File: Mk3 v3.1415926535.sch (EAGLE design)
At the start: 150 parts, among them IC1 TPD3E001DRL, IC2 TPS62082, IC3 STM32F401V, IC4 BQ24092, IC6 CC3100MOD, IC7 BQ2970, IC8 LSM6DS3, IC9 LIS3MDL, J1 ZX62-AB-5PA(11), J2 ER-CON50HT-1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

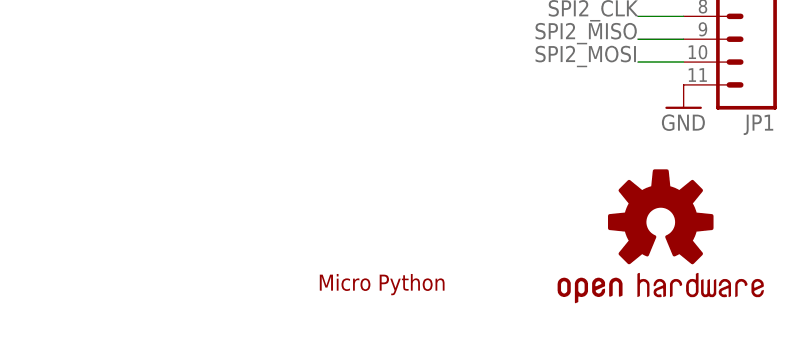
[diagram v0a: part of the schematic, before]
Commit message: Sponsor logos to rear Note this moves the files to Eagle 7
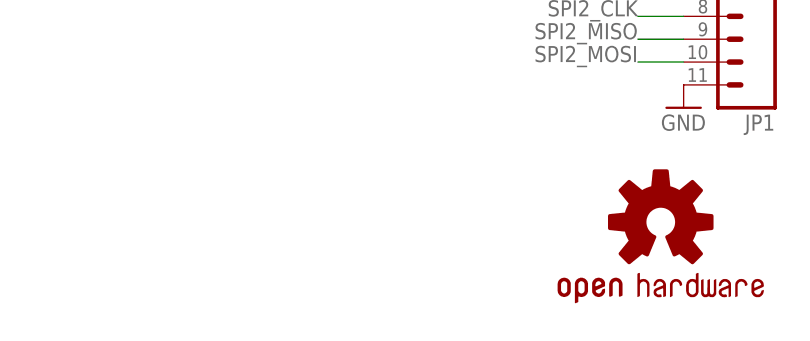
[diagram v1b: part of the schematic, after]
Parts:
- removed LOGO3: MICROPYTHON-SILK, TiLDA Mk3 Parts:MICROPYTHON-SILK
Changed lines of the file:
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@@
 <?xml version="1.0" encoding="utf-8"?>
 <!DOCTYPE eagle SYSTEM "eagle.dtd">
-<eagle version="6.6.0">
+<eagle version="7.5.0">
 <drawing>
 <settings>
@@
 <setting verticaltext="up"/>
 </settings>
-<grid distance="0.1" unitdist="inch" unit="inch" style="lines" multiple="1" display="no" altdistance="0.025" altunitdist="inch" altunit="inch"/>
+<grid distance="0.1" unitdist="inch" unit="inch" style="lines" multiple="1" display="no" altdistance="0.01" altunitdist="inch" altunit="inch"/>
 <layers>
 <layer number="1" name="Top" color="4" fill="1" visible="no" active="no"/>
@@
 <part name="+3V21" library="supply1" deviceset="+3V3" device=""/>
 <part name="OUTLINE1" library="TiLDA Mk3 Parts" deviceset="TILDA_MK3_BOARDOUTLINE" device="">
-<variant name="L4" populate="no"/>
-</part>
-<part name="LOGO3" library="TiLDA Mk3 Parts" deviceset="MICROPYTHON" device="-SILK" value="MICROPYTHON-SILK">
 <variant name="L4" populate="no"/>
 </part>
@@
 <instance part="+3V21" gate="G$1" x="210.82" y="40.64" rot="R90"/>
 <instance part="OUTLINE1" gate="G$1" x="502.92" y="27.94"/>
-<instance part="LOGO3" gate="G$1" x="292.1" y="7.62"/>
 <instance part="U2" gate="G$1" x="718.82" y="185.42"/>
 <instance part="R32" gate="G$1" x="647.7" y="134.62" smashed="yes" rot="R90">

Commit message: Lots of clean up in schematic
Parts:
- added LOGO2: LOGO_TI-4MM, TiLDA Mk3 Parts:LOGO_TI-4MM
- added LOGO3: LOGO_ST-4MM, TiLDA Mk3 Parts:LOGO_ST-4MM
- added LOGO4: LOGO_HCD-4MM, TiLDA Mk3 Parts:LOGO_HCD-4MM
- added LOGO5: LOGO_MICROSOFT-4MM, TiLDA Mk3 Parts:LOGO_MICROSOFT-4MM
- added LOGO6: LOGO_MICROPYTHON-8MM, TiLDA Mk3 Parts:LOGO_MICROPYTHON-8MM
- C27, C5, C6: device passives-7351:CAPACITOR0805-N -> TiLDA Mk3 Parts:C-EUC0805-N
- D1: device SparkFun-LED:WS2812B -> TiLDA Mk3 Parts:WS2812B
- D2, D3: device Diodes:1N4148-SOD123 -> TiLDA Mk3 Parts:1N4148-SOD123
- IC3: value STM32F401V -> STM32L475VG
- J3: value SWD_SHROUD-PINHEAD -> 2x5 1.27mm
- JP1, JP2: device SparkFun-Connectors:M11PTH -> TiLDA Mk3 Parts:M11PTH
- JP4: device tag-connect:TC2030-SWDNL -> TiLDA Mk3 Parts:TC2030-SWDNL
- LED2, LED4, LED5: value RED -> 0603 RED
- LED3: value GREEN -> 0603 GREEN
- R7: value DNP or 0 -> DNP or 0603/0R/5%
- S1, S7: value SWITCH-MOMENTARY-2SMD-1101NE -> 6x3; device SparkFun-Electromechanical:SWITCH-MOMENTARY-2SMD-1101NE -> TiLDA Mk3 Parts:SWITCH-MOMENTARY-2-SMD-1101NE
- S3, S4: value 1217769 -> SKPMAPE010
- S8: value DNP -> DNP (6x3); device SparkFun-Electromechanical:SWITCH-MOMENTARY-2SMD-1101NE -> TiLDA Mk3 Parts:SWITCH-MOMENTARY-2-SMD-1101NE
- SJ1: value JUMPER-PAD-2-NOYES_SILK -> SOLDERJUMPERNO; device SparkFun-Passives:JUMPER-PAD-2-NOYES_SILK -> TiLDA Mk3 Parts:SOLDERJUMPERNO
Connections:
- net BOOT0 renamed BOOT0/JOY_CEN
- net N$1 renamed DRDY
- net N$22 renamed C1
- net N$38 renamed VACP2
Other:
- note added: "(PARALLEL)"
- note added: "A"
- note added: "B"
- note added: "Front Buttons"
- note added: "IMU"
- note added: "LEDs"
- note added: "Piezo"
- note removed: "/ JOY_CEN"
- note removed: "/JOY_CENTRE"
- note removed: "DONE:"
- note removed: "LCD_CS (PARALLEL)"
- note removed: "List of things to check"
- note removed: "SDIO_SW can be easily changed away from pin PC13"
- note removed: "UI"
- note removed: "WS2812B"
- note removed: "add current measuring options"
- note removed: "aref arrangment, consider to allow Aref changing on gpio"
- note removed: "change footprint once final part is known"
- note removed: "check DMA channel conflicts"
- note removed: "is the stm32f4 annoying with interrupts on some pins, and are peripherals which require interrupt wired to take this into account?"
- note removed: "low ESR"
- note removed: "move esp decoupling cap to vcc pin"
- note removed: "orginally 1K, check to see if value is important"
- note removed: "potentially not needed, depends on STM32 pullups"
- note removed: "pull PB2 (BOOT1) low?"
- note removed: "see if a resistor is needed on the stm32 crytal"
- note removed: "shouldnt be needed"
- note removed: "sort out power switch"
- moved on the sheet: C10, C11, C12, C13, C15, C16, C17, C18, C19, C2, C22, C23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

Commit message: More clean up
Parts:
- IC6: value CC3100MOD -> CC3100MOD-LWK; device TiLDA Mk3 Parts:CC3100MOD -> TiLDA Mk3 Parts:CC3100MOD-LWK
- SW1: value JOYSTICK_MINI_MULTICOMP -> JOYSTICK_MINI_MULTICOM_NOSILK; device TiLDA Mk3 Parts:JOYSTICK_MINI_MULTICOMP -> TiLDA Mk3 Parts:JOYSTICK_MINI_MULTICOM_NOSILK
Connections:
- net N$13 renamed BAT
- net N$2 renamed SW
- net N$50 renamed COUT
- net N$54 renamed VBAT_SWITCH_CONTROL
- net N$55 renamed DOUT
- net N$63 renamed V-
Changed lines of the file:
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@@
 <setting verticaltext="up"/>
 </settings>
-<grid distance="0.1" unitdist="inch" unit="inch" style="lines" multiple="1" display="no" altdistance="0.05" altunitdist="inch" altunit="inch"/>
+<grid distance="0.1" unitdist="inch" unit="inch" style="lines" multiple="1" display="no" altdistance="0.01" altunitdist="inch" altunit="inch"/>
 <layers>
 <layer number="1" name="Top" color="4" fill="1" visible="yes" active="no"/>
@@
 <layer number="19" name="Unrouted" color="6" fill="1" visible="yes" active="no"/>
 <layer number="20" name="Dimension" color="15" fill="1" visible="yes" active="no"/>
-<layer number="21" name="tPlace" color="6" fill="1" visible="yes" active="no"/>
-<layer number="22" name="bPlace" color="15" fill="1" visible="yes" active="no"/>
+<layer number="21" name="tPlace" color="7" fill="1" visible="yes" active="no"/>
+<layer number="22" name="bPlace" color="6" fill="1" visible="yes" active="no"/>
 <layer number="23" name="tOrigins" color="15" fill="1" visible="yes" active="no"/>
 <layer number="24" name="bOrigins" color="15" fill="1" visible="yes" active="no"/>
 <layer number="25" name="tNames" color="7" fill="1" visible="yes" active="no"/>
-<layer number="26" name="bNames" color="7" fill="1" visible="yes" active="no"/>
+<layer number="26" name="bNames" color="6" fill="1" visible="yes" active="no"/>
 <layer number="27" name="tValues" color="7" fill="1" visible="yes" active="no"/>
 <layer number="28" name="bValues" color="7" fill="1" visible="yes" active="no"/>
@@
 <part name="GND46" library="TiLDA Mk3 Parts" deviceset="GND" device=""/>
 <part name="+3V4" library="TiLDA Mk3 Parts" deviceset="+3V3" device=""/>
-<part name="SW1" library="TiLDA Mk3 Parts" deviceset="JOYSTICK_MINI" device="_MULTICOMP">
+<part name="SW1" library="TiLDA Mk3 Parts" deviceset="JOYSTICK_MINI" device="_MULTICOM_NOSILK" value="JOYSTICK_MINI_MULTICOM_NOSILK">
 <attribute name="FARNELL" value="1316987"/>
 </part>
@@
 <attribute name="EBAY" value="272150658613"/>
 </part>
-<part name="IC6" library="TiLDA Mk3 Parts" deviceset="CC3100MOD" device="">
+<part name="IC6" library="TiLDA Mk3 Parts" deviceset="CC3100MOD" device="-LWK" value="CC3100MOD-LWK">
 <attribute name="MOUSER" value="  595-3100MODR11MAMOBR"/>
 </part>
@@
 </segment>
 </net>
-<net name="N$54" class="0">
+<net name="VBAT_SWITCH_CONTROL" class="0">
 <segment>
 <pinref part="R45" gate="G$1" pin="2"/>
@@
 </segment>
 </net>
-<net name="N$50" class="0">
+<net name="COUT" class="0">
 <segment>
 <pinref part="IC7" gate="G$1" pin="COUT"/>
@@
 <wire x1="568.96" y1="134.62" x2="574.04" y2="134.62" width="0.1524" layer="91"/>
 <junction x="574.04" y="134.62"/>
+<label x="581.66" y="137.16" size="1.778" layer="95" rot="MR270"/>
 </segment>
 </net>
-<net name="N$55" class="0">
+<net name="DOUT" class="0">
 <segment>
 <pinref part="IC7" gate="G$1" pin="DOUT"/>
@@
 <wire x1="599.44" y1="134.62" x2="599.44" y2="132.08" width="0.1524" layer="91"/>
 <junction x="594.36" y="134.62"/>
+<label x="586.74" y="137.16" size="1.778" layer="95" rot="MR270"/>
 </segment>
 </net>
@@
 <junction x="650.24" y="142.24"/>
 <label x="657.86" y="142.24" size="1.778" layer="95" rot="MR0"/>
+<label x="601.98" y="147.32" size="1.778" layer="95"/>
 </segment>
 </net>
-<net name="N$63" class="0">
+<net name="V-" class="0">
 <segment>
 <pinref part="IC7" gate="G$1" pin="V-"/>
@@
 <pinref part="R50" gate="G$1" pin="1"/>
 <wire x1="561.34" y1="147.32" x2="561.34" y2="132.08" width="0.1524" layer="91"/>
+<label x="566.42" y="147.32" size="1.778" layer="95" rot="MR0"/>
 </segment>
 </net>
@@
 </segment>
 </net>
-<net name="N$2" class="0">
+<net name="SW" class="0">
 <segment>
 <pinref part="L1" gate="G$1" pin="1"/>
@@
 </segment>
 </net>
-<net name="N$13" class="0">
+<net name="BAT" class="0">
 <segment>
 <pinref part="IC7" gate="G$1" pin="BAT"/>
@@
 <wire x1="599.44" y1="154.94" x2="607.06" y2="154.94" width="0.1524" layer="91"/>
 <wire x1="607.06" y1="154.94" x2="609.6" y2="154.94" width="0.1524" layer="91"/>
+<label x="601.98" y="154.94" size="1.778" layer="95"/>
 </segment>
 </net>
